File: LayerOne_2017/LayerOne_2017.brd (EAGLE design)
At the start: 73.6 x 73.7 mm, 70 parts, among them IC1 STM32F446_LQFP64, IC2 REG1117, J1 SPI_TFT_DISPLAY, Q1 2N2222, Q2 MMBT2222A, U1 SN65HVD235DR, U2 SN65HVD235DR, U4 SDCARD, U5 FERRITE0805, X1 STEREOJACK, X2 MINI-USB-32005-301

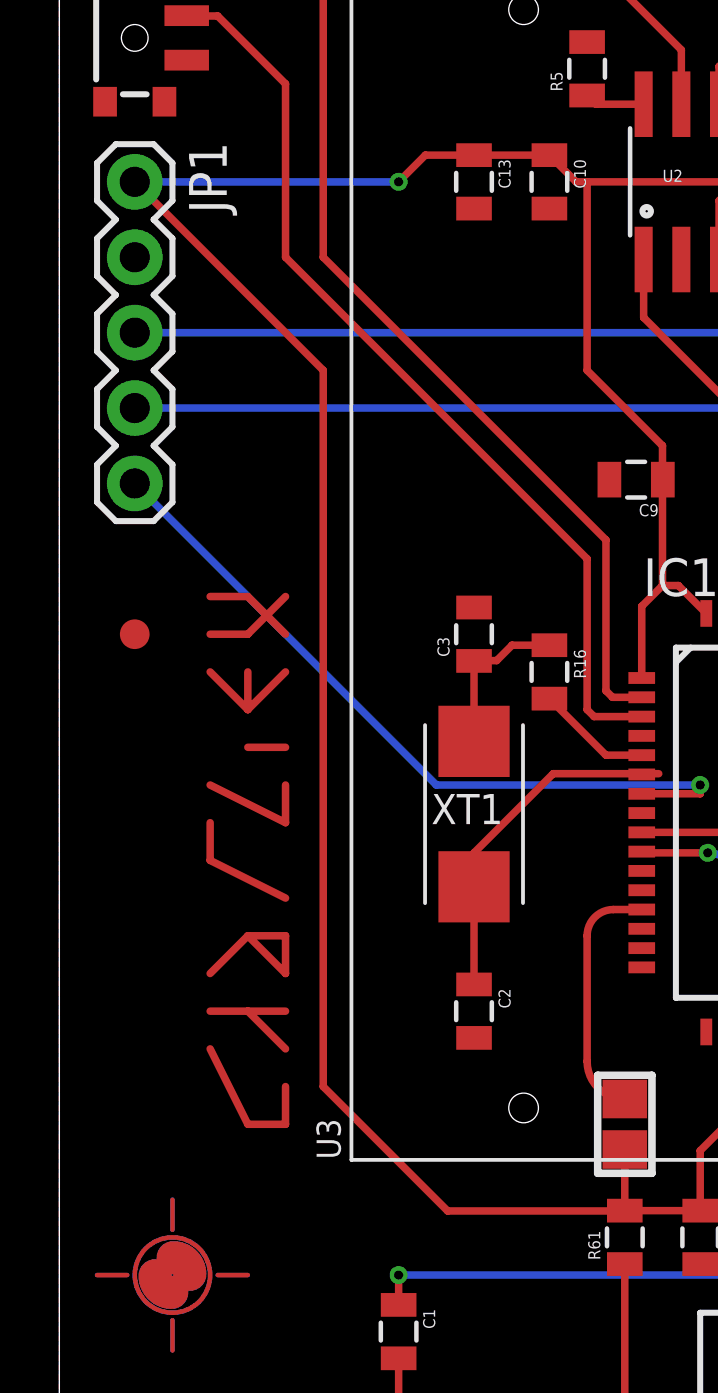
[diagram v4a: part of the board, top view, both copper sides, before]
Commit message: added reset switch
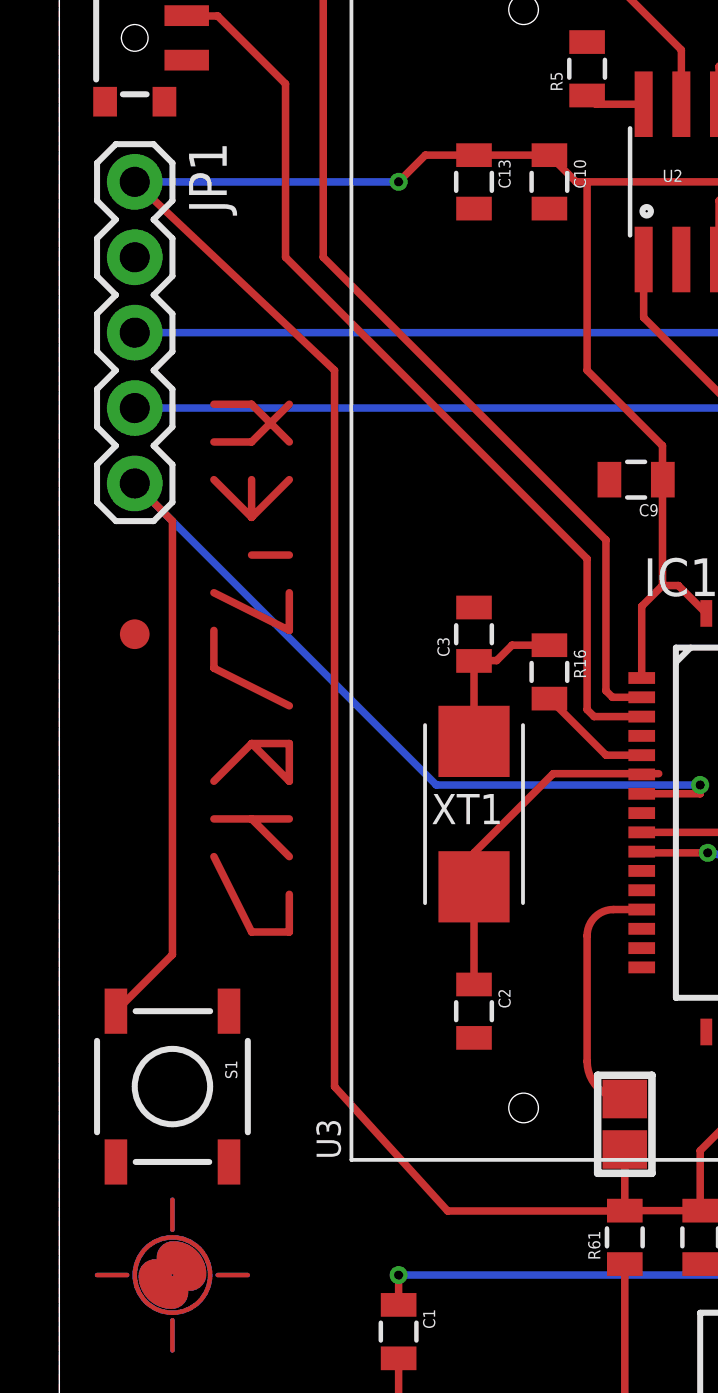
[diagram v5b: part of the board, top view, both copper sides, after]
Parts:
- added S1: (no value), Nullspace:SPARKFUN_TACTILE_SWITCH_SMD
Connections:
- net GND: now also S1.1
- net NRST: now also S1.3
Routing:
- net NRST: track 25.5 -> 44.6 mm
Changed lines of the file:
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@@
 <element name="SW1" library="microbuilder" package="SPST_SMT_19192" value="" x="10.16" y="69.85" rot="R180"/>
 <element name="SW2" library="microbuilder" package="SPST_SMT_19192" value="" x="2.54" y="60.96" rot="R270"/>
+<element name="S1" library="Nullspace" package="SPARKFUN_TACTILE_SWITCH_SMD" value="" x="3.81" y="24.13" rot="R270"/>
 </elements>
 <signals>
@@
 <wire x1="24.13" y1="20.32" x2="27.57" y2="20.32" width="0.254" layer="1"/>
 <wire x1="27.57" y1="20.32" x2="27.94" y2="19.95" width="0.254" layer="1"/>
-<wire x1="13.081" y1="19.939" x2="8.89" y2="24.13" width="0.254" layer="1"/>
-<wire x1="8.89" y1="24.13" x2="8.89" y2="48.26" width="0.254" layer="1"/>
-<wire x1="8.89" y1="48.26" x2="2.54" y2="54.61" width="0.254" layer="1"/>
+<wire x1="13.081" y1="19.939" x2="9.271" y2="24.13" width="0.254" layer="1"/>
+<wire x1="9.271" y1="24.13" x2="9.271" y2="48.26" width="0.254" layer="1"/>
+<wire x1="9.271" y1="48.26" x2="2.54" y2="54.61" width="0.254" layer="1"/>
 <wire x1="13.97" y1="55.51" x2="12.33" y2="55.51" width="0.254" layer="1"/>
 <wire x1="12.33" y1="55.51" x2="11.43" y2="54.61" width="0.254" layer="1"/>
@@
 <contactref element="SW1" pad="C"/>
 <contactref element="SW2" pad="C"/>
+<contactref element="S1" pad="1"/>
 <wire x1="35.56" y1="42.81" x2="33.72" y2="37.245" width="0" layer="19" extent="1-1"/>
 <wire x1="20.955" y1="51.9938" x2="16.51" y2="53.71" width="0" layer="19" extent="1-1"/>
@@
 <wire x1="21.59" y1="34.29" x2="12.7" y2="34.29" width="0.254" layer="16"/>
 <wire x1="12.7" y1="34.29" x2="2.54" y2="44.45" width="0.254" layer="16"/>
+<contactref element="S1" pad="3"/>
+<wire x1="1.905" y1="26.67" x2="3.81" y2="28.575" width="0.254" layer="1"/>
+<wire x1="3.81" y1="28.575" x2="3.81" y2="43.18" width="0.254" layer="1"/>
+<wire x1="3.81" y1="43.18" x2="2.54" y2="44.45" width="0.254" layer="1"/>
 </signal>
 <signal name="SELECT0">
@@
 </signal>
 <signal name="N$5">
-<wire x1="5.08" y1="26.67" x2="6.35" y2="26.67" width="0.254" layer="1"/>
-<wire x1="7.62" y1="25.4" x2="6.35" y2="26.67" width="0.254" layer="1"/>
-<wire x1="6.35" y1="26.67" x2="7.62" y2="26.67" width="0.254" layer="1"/>
+<wire x1="5.207" y1="33.147" x2="6.477" y2="33.147" width="0.254" layer="1"/>
+<wire x1="7.747" y1="31.877" x2="6.477" y2="33.147" width="0.254" layer="1"/>
+<wire x1="6.477" y1="33.147" x2="7.747" y2="33.147" width="0.254" layer="1"/>
 </signal>
 <signal name="N$7">
-<wire x1="7.62" y1="27.94" x2="7.62" y2="29.21" width="0.254" layer="1"/>
-<wire x1="7.62" y1="29.21" x2="6.35" y2="29.21" width="0.254" layer="1"/>
-<wire x1="6.35" y1="29.21" x2="5.08" y2="27.94" width="0.254" layer="1"/>
-<wire x1="7.62" y1="27.94" x2="6.35" y2="29.21" width="0.254" layer="1"/>
+<wire x1="7.747" y1="34.417" x2="7.747" y2="35.687" width="0.254" layer="1"/>
+<wire x1="7.747" y1="35.687" x2="6.477" y2="35.687" width="0.254" layer="1"/>
+<wire x1="6.477" y1="35.687" x2="5.207" y2="34.417" width="0.254" layer="1"/>
+<wire x1="7.747" y1="34.417" x2="6.477" y2="35.687" width="0.254" layer="1"/>
 </signal>
 <signal name="N$8">
-<wire x1="5.08" y1="25.4" x2="6.35" y2="22.86" width="0.254" layer="1"/>
-<wire x1="6.35" y1="22.86" x2="7.62" y2="22.86" width="0.254" layer="1"/>
-<wire x1="7.62" y1="22.86" x2="7.62" y2="24.13" width="0.254" layer="1"/>
+<wire x1="5.207" y1="31.877" x2="6.477" y2="29.337" width="0.254" layer="1"/>
+<wire x1="6.477" y1="29.337" x2="7.747" y2="29.337" width="0.254" layer="1"/>
+<wire x1="7.747" y1="29.337" x2="7.747" y2="30.607" width="0.254" layer="1"/>
 </signal>
 <signal name="N$9">
-<wire x1="7.62" y1="30.48" x2="5.08" y2="31.75" width="0.254" layer="1"/>
-<wire x1="5.08" y1="31.75" x2="5.08" y2="33.02" width="0.254" layer="1"/>
+<wire x1="7.747" y1="36.957" x2="5.207" y2="38.227" width="0.254" layer="1"/>
+<wire x1="5.207" y1="38.227" x2="5.207" y2="39.497" width="0.254" layer="1"/>
 </signal>
 <signal name="N$11">
-<wire x1="5.08" y1="34.29" x2="7.62" y2="33.02" width="0.254" layer="1"/>
-<wire x1="7.62" y1="33.02" x2="7.62" y2="34.29" width="0.254" layer="1"/>
+<wire x1="5.207" y1="40.767" x2="7.747" y2="39.497" width="0.254" layer="1"/>
+<wire x1="7.747" y1="39.497" x2="7.747" y2="40.767" width="0.254" layer="1"/>
 </signal>
 <signal name="N$12">
-<wire x1="6.35" y1="35.56" x2="7.62" y2="35.56" width="0.254" layer="1"/>
+<wire x1="6.477" y1="42.037" x2="7.747" y2="42.037" width="0.254" layer="1"/>
 </signal>
 <signal name="N$20">
-<wire x1="6.35" y1="36.83" x2="7.62" y2="38.1" width="0.254" layer="1"/>
-<wire x1="6.35" y1="36.83" x2="5.08" y2="38.1" width="0.254" layer="1"/>
-<wire x1="6.35" y1="36.83" x2="6.35" y2="38.1" width="0.254" layer="1"/>
+<wire x1="6.477" y1="43.307" x2="7.747" y2="44.577" width="0.254" layer="1"/>
+<wire x1="6.477" y1="43.307" x2="5.207" y2="44.577" width="0.254" layer="1"/>
+<wire x1="6.477" y1="43.307" x2="6.477" y2="44.577" width="0.254" layer="1"/>
 </signal>
 <signal name="N$21">
-<wire x1="5.08" y1="39.37" x2="6.35" y2="39.37" width="0.254" layer="1"/>
-<wire x1="6.35" y1="39.37" x2="7.62" y2="40.64" width="0.254" layer="1"/>
-<wire x1="7.62" y1="39.37" x2="6.35" y2="40.64" width="0.254" layer="1"/>
-<wire x1="6.35" y1="40.64" x2="5.08" y2="40.64" width="0.254" layer="1"/>
-<wire x1="5.08" y1="39.37" x2="5.08" y2="40.64" width="0" layer="19" extent="1-1"/>
+<wire x1="5.207" y1="45.847" x2="6.477" y2="45.847" width="0.254" layer="1"/>
+<wire x1="6.477" y1="45.847" x2="7.747" y2="47.117" width="0.254" layer="1"/>
+<wire x1="7.747" y1="45.847" x2="6.477" y2="47.117" width="0.254" layer="1"/>
+<wire x1="6.477" y1="47.117" x2="5.207" y2="47.117" width="0.254" layer="1"/>
+<wire x1="7.747" y1="45.847" x2="6.477" y2="45.847" width="0" layer="19" extent="1-1"/>
 </signal>
 <signal name="N$23">

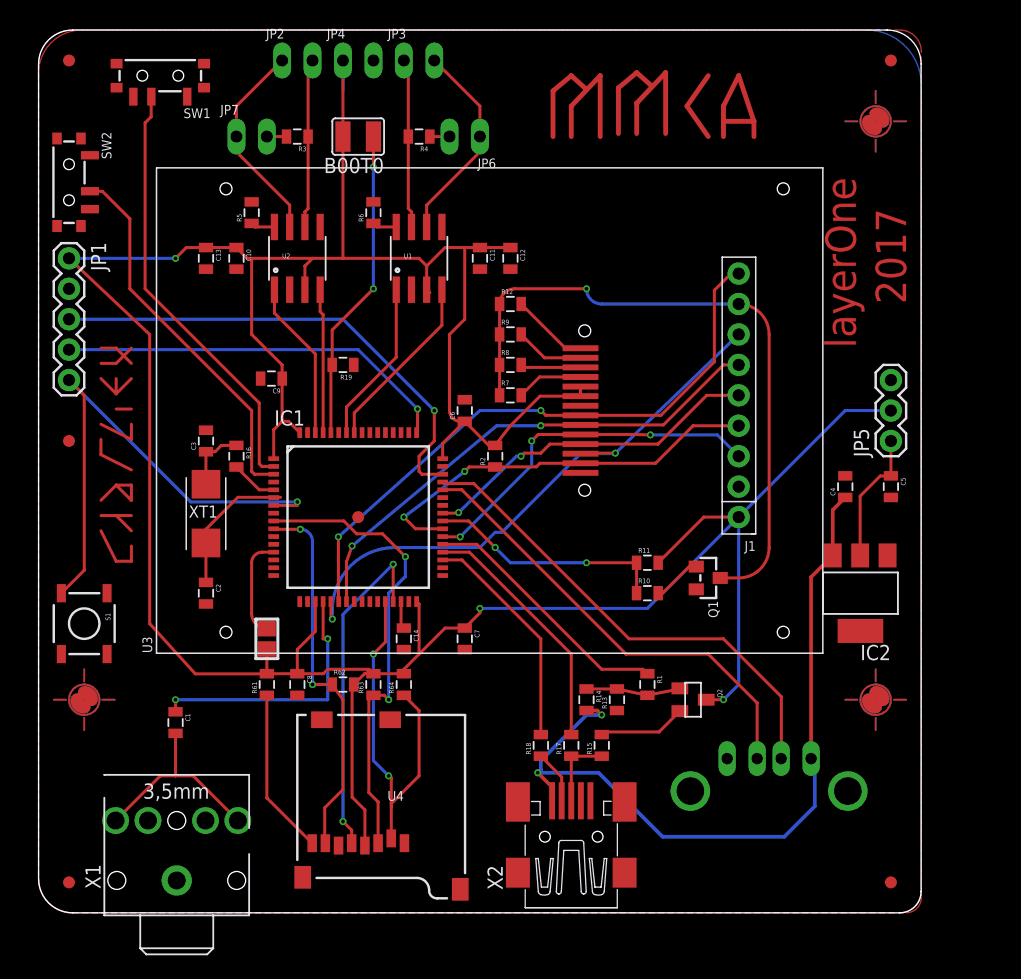
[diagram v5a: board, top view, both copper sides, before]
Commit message: cpu updated.
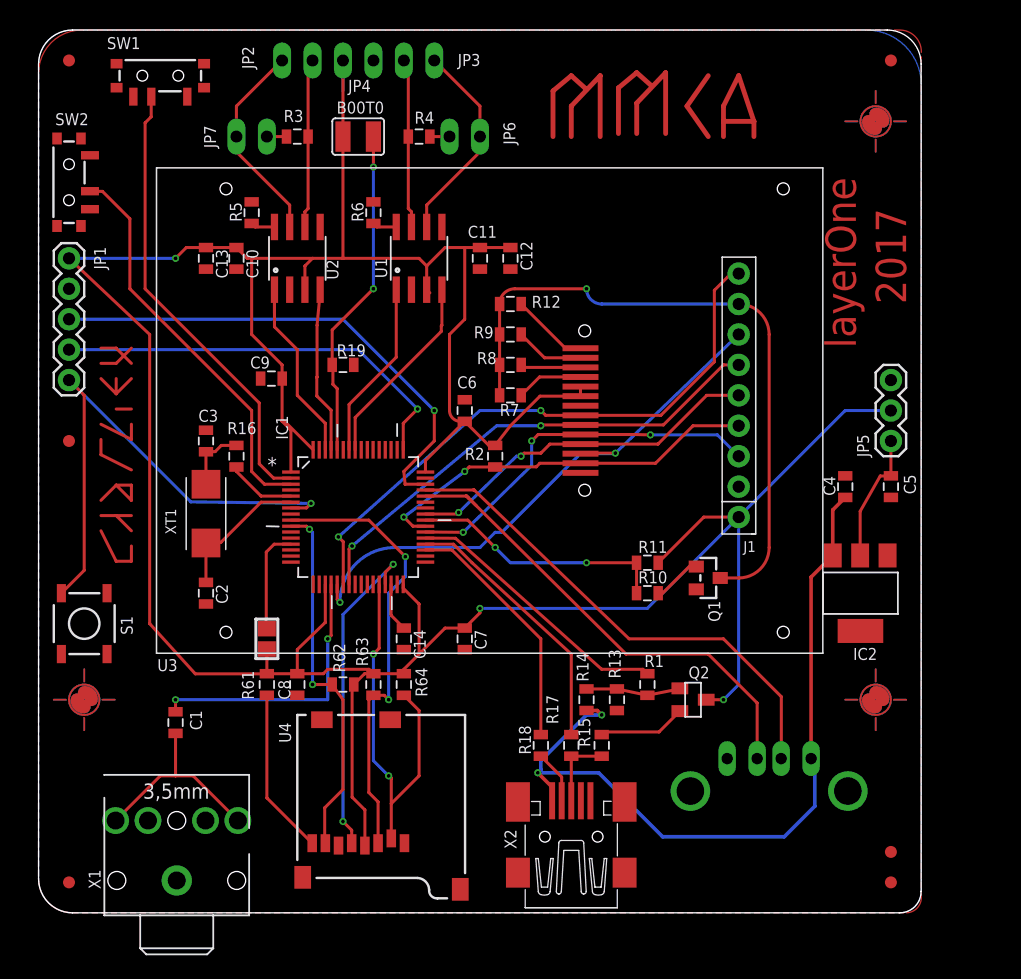
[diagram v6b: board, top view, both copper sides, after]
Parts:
- IC1: value STM32F446_LQFP64 -> STM32F446_LQFP64LQFP64; device stm32f466re:LQFP64_PACKAGE -> stm32f466re:LQFP64
- moved U$5 52.5 mm to (71.1, 5.08)
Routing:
- net +3V3: track 277.0 -> 285.3 mm
- net CAN1_TX: track 13.3 -> 17.1 mm
- net D-: track 38.3 -> 40.8 mm
- net SYS_JTCK-SWCLK: track 33.1 -> 35.0 mm
- net N$19: track 3.90 -> 5.77 mm
- net CAN1_RX: track 12.0 -> 13.9 mm
- net SELECT0: track 36.1 -> 37.9 mm
- net N$2: track 2.31 -> 4.09 mm
- net USB_OTG_HS_DM: track 18.9 -> 20.7 mm
- net SELECT1: track 31.5 -> 33.3 mm
- net TFT_SCK: track 48.5 -> 47.0 mm
- net B00T0: track 26.2 -> 27.7 mm
- net USB_OTG_HS_DP: track 21.0 -> 22.5 mm
- net TFT_RESET: track 34.4 -> 32.9 mm
- net TFT_DC: track 28.7 -> 30.2 mm
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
